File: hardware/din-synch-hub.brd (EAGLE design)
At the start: 160 x 100 mm, 47 parts, among them IC1 6N138, IC2 PIC12F1822SO08, IC3 4050D, IC4 REG1117, IC6 4050D, X1 DIN5PIN, X2 DIN5PIN, X3 DIN5PIN, X4 DIN5PIN, X5 DIN5PIN, X6 DIN5PIN

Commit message: ready for fab
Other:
- board size 160 x 100 mm -> 140.7 x 20.2 mm
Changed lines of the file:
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@@
 <board>
 <plain>
-<wire x1="0" y1="0" x2="160" y2="0" width="0" layer="20"/>
-<wire x1="160" y1="0" x2="160" y2="100" width="0" layer="20"/>
-<wire x1="160" y1="100" x2="0" y2="100" width="0" layer="20"/>
-<wire x1="0" y1="100" x2="0" y2="0" width="0" layer="20"/>
 <wire x1="7.112" y1="43.688" x2="131.064" y2="43.688" width="0.4064" layer="20"/>
 <wire x1="7.747" y1="23.495" x2="145.415" y2="23.495" width="0.4064" layer="20"/>

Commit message: updates
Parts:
- C3: device rcl:C0805 -> rcl:E2,5-6E
- C7: device rcl:E2,5-6E -> rcl:C0805
- moved R15 123.6 mm to (125.7, 4.32), turned to 270 degrees
- moved R16 103.6 mm to (133.5, 4.32), turned to 270 degrees
- moved R14 100.2 mm to (113.7, 4.32), turned to 270 degrees
- moved R13 90.4 mm to (106.0, 4.32), turned to 270 degrees
- moved R10 50.5 mm to (74.3, 4.32)
- moved R11 50.5 mm to (86.4, 4.32)
- moved R12 50.5 mm to (94.0, 4.32)
- moved R8 50.5 mm to (54.7, 4.32)
- moved R5 50.4 mm to (27.3, 4.32)
- moved R6 50.4 mm to (35.1, 4.32)
- moved R9 50.4 mm to (66.7, 4.32)
- moved R7 50.4 mm to (47.0, 4.32)
- moved C1 46.7 mm to (21.0, 7.11), turned to 180 degrees
- moved R2 42.6 mm to (1.91, 9.65), turned to 90 degrees
- moved C5 42.6 mm to (78.7, 12.2), turned to 270 degrees
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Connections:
- net GND: now also C3.-, C5.2, C7.1, R3.2, R4.1; no longer C3.2, C5.1, C7.-, R14.2, R16.1
- net IN: now also R1.1; no longer R15.1
- net N$1: now also R6.1; no longer R1.1
- net N$10: now also R10.2; no longer R5.2
- net N$11: now also R9.2; no longer R6.2
- net N$12: now also R9.1; no longer R6.1
- net N$13: now also R12.1; no longer R7.1
- net N$14: now also R12.2; no longer R7.2
- net N$15: now also R11.1; no longer R8.1
- net N$16: now also R11.2; no longer R8.2
- net N$17: now also R14.1; no longer R9.1
- net N$18: now also R14.2; no longer R9.2
- net N$19: now also R13.1; no longer R10.1
- net N$2: now also R6.2; no longer R1.2
- net N$20: now also R13.2; no longer R10.2
- net N$21: now also R16.1; no longer R11.1
- net N$22: now also R16.2; no longer R11.2
- net N$23: now also R15.2; no longer R12.2
- net N$24: now also R15.1; no longer R12.1
- net N$26: now also R2.1; no longer R13.1
- net N$27: now also R2.2; no longer R13.2
- net N$29: now also R3.1; no longer R14.1
- net N$3: now also R5.1; no longer R2.1
- net N$30: now also R4.2; no longer R16.2
- net N$32: now also C3.+; no longer C6.+
- net N$4: now also R5.2; no longer R2.2
- net N$5: now also R8.1; no longer R3.1
- net N$6: now also R8.2; no longer R3.2
- net N$7: now also R7.1; no longer R4.1
- net N$8: now also R7.2; no longer R4.2
- net N$9: now also R10.1; no longer R5.1
- net VCC: now also C5.1, C6.+, C7.2, R1.2; no longer C3.1, C5.2, C7.+, R15.2
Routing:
- net N$5: track 7.82 -> 20.0 mm, vias 0 -> 2
- net N$9: track 20.9 -> 31.9 mm, vias 0 -> 2
- net N$21: track 22.7 -> 32.2 mm
- net N$3: track 12.9 -> 22.3 mm, vias 0 -> 2
- net N$17: track 8.56 -> 17.8 mm, vias 0 -> 2
- net N$15: track 11.4 -> 19.7 mm, vias 0 -> 2
- net N$12: track 32.1 -> 24.6 mm
- net N$24: track 33.7 -> 27.9 mm, vias 0 -> 2
- net N$13: track 20.5 -> 15.3 mm
- net N$1: track 21.7 -> 16.9 mm
- net N$26: track 6.19 -> 9.55 mm
- net CLK: track 115.1 -> 112.2 mm, vias 7 -> 6
- net N$16: track 3.87 -> 6.74 mm
- net GND: track 191.3 -> 194.0 mm
- net RUN: track 123.9 -> 126.5 mm, vias 4 -> 5
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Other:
- board text added: "Sync Hole"
- board text added: "rev 2"
- board text removed: "DIN Sync Hub"
- board text removed: "rev 1"

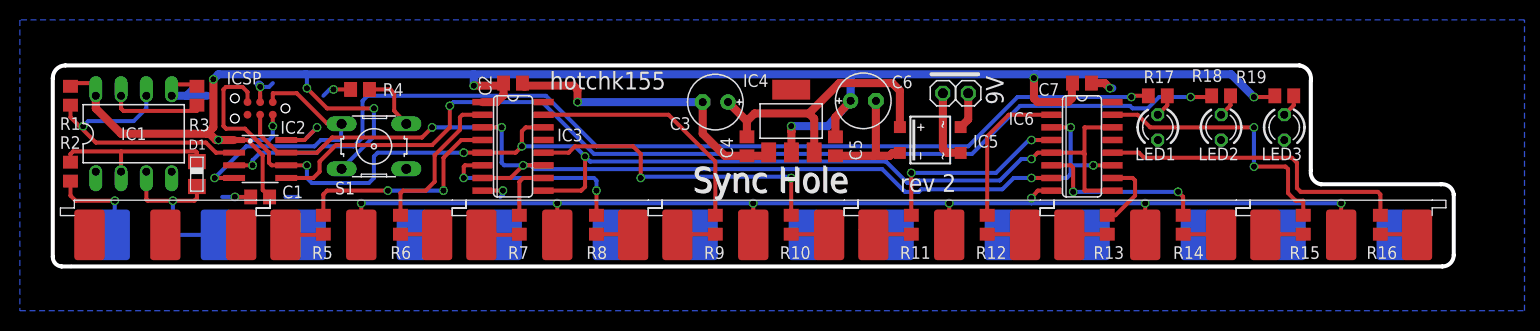
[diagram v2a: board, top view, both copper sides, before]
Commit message: added new power socket
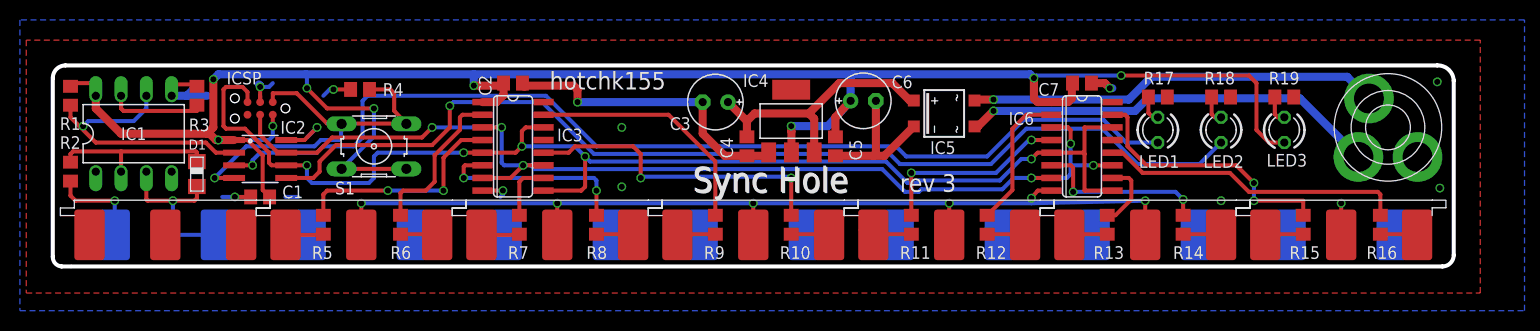
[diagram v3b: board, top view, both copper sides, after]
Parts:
- removed JP1, JP2: (no value), pinhead:1X01
- added U$1: PWR_SOCKET_2_1MM, jason_eagle6:PWR_SOCKET_2_1MM
- moved IC5 3.01 mm to (89.7, 15.5)
- moved LED1 0.25 mm to (111.1, 13.8), turned to 90 degrees
- moved LED2 0.25 mm to (117.5, 13.8), turned to 90 degrees
- moved LED3 0.25 mm to (123.8, 13.8), turned to 90 degrees
- moved R17 0.13 mm to (111.1, 17.1)
- moved R18 0.13 mm to (117.5, 17.1)
- moved R19 0.13 mm to (123.8, 17.1)
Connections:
- net GND: now also R17.1, R18.1, R19.1; no longer LED1.K, LED2.K, LED3.K
- net LED1: now also LED1.A; no longer R17.2
- net LED2: now also LED2.A; no longer R18.2
- net N$28: now also LED3.K, R19.2; no longer LED3.A, R19.1
- net N$31: now also LED2.K, R18.2; no longer LED1.A, R17.1
- net N$33: now also LED1.K, R17.2; no longer LED2.A, R18.1
- net N$36: now also U$1.PIN; no longer JP1.1
- net N$37: now also U$1.BARREL; no longer JP2.1
- net VCC: now also LED3.A; no longer R19.2
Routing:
- net N$36: track 3.71 -> 41.5 mm, vias 0 -> 1
- net N$37: track 7.58 -> 42.2 mm, vias 0 -> 1
- net GND: track 194.0 -> 177.1 mm, vias 14 -> 19
- net VCC: track 200.3 -> 212.2 mm
- net N$30: track 33.9 -> 40.5 mm
- net LED2: track 102.8 -> 105.3 mm, vias 2 -> 1
- net N$32: track 29.3 -> 27.5 mm
- net LED1: track 101.4 -> 103.1 mm, vias 2 -> 1
- net N$21: track 32.2 -> 30.7 mm
- net N$13: track 15.3 -> 14.2 mm
- net N$24: track 27.9 -> 26.9 mm
- net N$19: track 7.50 -> 6.96 mm
- added copper zone on layer 1, net GND
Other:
- outline, holes or cut-outs redrawn
- board text added: "rev 3"
- board text removed: "9V"
- board text removed: "rev 2"

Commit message: major changes
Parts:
- added X7: VERTICAL_3_5MM_SOCKET, jason_eagle6:VERTICAL_3_5MM_SOCKET
- C3: device rcl:E2,5-6E -> rcl:C0805
- C7: device rcl:C0805 -> rcl:E2,5-6E
- IC1: value 6N138 -> 4050D; device optocoupler:DIL08 -> 40xx:SO16
- IC2: value PIC12F1822SO08 -> REG1117; device jasons_stuff:SO08 -> burr-brown:SOT223
- IC4: value REG1117 -> PIC12F1822SO08; device burr-brown:SOT223 -> jasons_stuff:SO08
- IC5: value (none) -> 6N138; device microbuilder:SOIC-4 -> optocoupler:DIL08
- IC6: value 4050D -> (none); device 40xx:SO16 -> microbuilder:SOIC-4
- moved R1 121.9 mm to (123.8, 17.1), flipped to the bottom, turned to 180 degrees
- moved R19 120.9 mm to (3.17, 9.65), flipped to the bottom, turned to 90 degrees
- moved R2 115.8 mm to (117.5, 17.1), flipped to the bottom, turned to 180 degrees
- moved R5 110.5 mm to (137.8, 3.94), flipped to the bottom
- moved R16 110.3 mm to (23.7, 15.8), flipped to the bottom, turned to 90 degrees
- moved R3 96.5 mm to (111.1, 17.1), flipped to the bottom, turned to 180 degrees
- moved R18 95.4 mm to (22.4, 8.29), flipped to the bottom, turned to 90 degrees
- moved R17 86.4 mm to (25.0, 10.4), flipped to the bottom, turned to 270 degrees
- moved R15 86.4 mm to (39.4, 3.91), flipped to the bottom
- moved R6 86.2 mm to (121.3, 3.94), flipped to the bottom
- moved IC1 83.8 mm to (92.1, 12.2), flipped to the bottom, turned to 270 degrees
- moved C1 72.0 mm to (92.1, 18.5), flipped to the bottom
- moved R4 72.0 mm to (103.0, 17.8), flipped to the bottom, turned to 90 degrees
- moved R14 71.2 mm to (42.5, 3.94), flipped to the bottom
- moved R7 71.1 mm to (118.1, 3.94), flipped to the bottom
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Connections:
- removed net IN: IC1.6, IC2.2, R1.1
- removed net N$24: IC6.15, R15.1
- new net MIDI: IC3.14, IC4.2, IC5.6, R16.1
- net CLK: now also IC1.3, IC1.7, IC1.9, IC4.7; no longer IC2.7, IC3.11, IC6.11, IC6.3, IC6.7
- net GND: now also C1.1, C2.1, C3.2, C4.2, C7.-, IC1.8, IC2.1, IC3.9, IC4.8, IC5.5, IC6.-, R1.1, R17.2, R2.1, R3.1, S1.1, S1.2; no longer C1.2, C2.2, C3.-, C4.1, C7.1, IC1.5, IC2.8, IC4.1, IC5.-, IC6.8, R17.1, R18.1, R19.1, R3.2, R4.1
- net LED1: now also IC4.3; no longer IC2.3
- net LED2: now also IC4.5; no longer IC2.5
- net N$1: now also IC3.15, R15.1; no longer IC3.2, R6.1
- net N$10: now also R11.2; no longer R10.2
- net N$11: now also R12.2; no longer R9.2
- net N$12: now also IC1.15, R10.1; no longer IC3.15, R9.1
- net N$13: now also IC1.12, R8.1; no longer IC6.2, R12.1
- net N$14: now also R9.2; no longer R12.2
- net N$15: now also IC1.10, R9.1; no longer IC6.4, R11.1
- net N$16: now also R10.2; no longer R11.2
- net N$17: now also IC1.2, R5.1; no longer IC6.6, R14.1
- net N$18: now also R7.2; no longer R14.2
- net N$19: now also IC1.4, R6.1; no longer IC6.10, R13.1
- net N$2: now also R15.2, X1.5; no longer R6.2, X1.3
- net N$20: now also R8.2; no longer R13.2
- net N$21: now also IC1.6, R7.1; no longer IC6.12, R16.1
- net N$22: now also R5.2; no longer R16.2
- net N$23: now also R6.2; no longer R15.2
- net N$25: now also IC5.3, X7.3; no longer IC1.3
- net N$26: now also R19.1, X7.4; no longer R2.1
- net N$27: now also IC5.2, R19.2; no longer IC1.2, R2.2
- net N$28: now also R1.2; no longer R19.2
- net N$29: now also IC5.7, R17.1; no longer IC1.7, R3.1
- net N$3: now also IC3.6, R13.1; no longer IC3.4, R5.1
- net N$30: now also IC4.4, R4.1; no longer IC2.4, R4.2
- net N$31: now also R2.2; no longer R18.2
- net N$32: now also C2.2, C7.+, IC2.3, IC6.+; no longer C3.+, C4.2, IC4.3, IC5.+
- net N$33: now also R3.2; no longer R17.2
- net N$36: now also IC6.~2; no longer IC5.~2
- net N$37: now also IC6.~1; no longer IC5.~1
- net N$4: now also R18.1; no longer R5.2
- net N$5: now also IC3.12, R14.1; no longer IC3.6, R8.1
- net N$6: now also R13.2; no longer R8.2
- net N$7: now also IC3.4, R12.1; no longer IC3.10, R7.1
- net N$8: now also R14.2; no longer R7.2
- net N$9: now also IC3.2, R11.1; no longer IC3.12, R10.1
- net RUN: now also IC1.11, IC1.14, IC1.5, IC3.11, IC4.6; no longer IC2.6, IC3.14, IC3.9, IC6.14, IC6.5, IC6.9
- net VCC: now also C1.2, C3.1, C4.1, IC1.1, IC2.2, IC4.1, IC5.8, R16.2, R18.2, R4.2; no longer C1.1, C2.1, C7.2, IC1.8, IC2.1, IC4.2, IC6.1, R1.2, S1.1, S1.2
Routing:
- net GND: track 177.1 -> 16.0 mm, vias 19 -> 12
- net MIDI: track 0.00 -> 48.9 mm, vias 0 -> 3
- net RUN: track 126.5 -> 78.0 mm, vias 5 -> 4
- net VCC: track 212.2 -> 167.7 mm, vias 9 -> 4
- net N$30: track 40.5 -> 83.6 mm, vias 1 -> 3
- net N$37: track 42.2 -> 8.75 mm, vias 1 -> 0
- net N$17: track 17.7 -> 51.1 mm, vias 2 -> 0
- net N$32: track 27.5 -> 57.8 mm, vias 0 -> 3
- net N$36: track 41.5 -> 11.2 mm, vias 1 -> 0
- net LED1: track 103.1 -> 73.5 mm
- net IN: track 27.9 -> 0.00 mm, vias 1 -> 0
- net N$24: track 26.9 -> 0.00 mm, vias 2 -> 0
- net N$19: track 6.96 -> 33.6 mm
- net CLK: track 112.0 -> 89.2 mm, vias 6 -> 8
- net N$26: track 9.55 -> 28.3 mm, vias 1 -> 0
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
